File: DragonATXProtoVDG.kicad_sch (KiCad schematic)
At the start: 69 parts, among them IC1 74LS273, IC2 MC6847, IC3 MC14053, J1 Video Output, J2 Board Interconnect Male, J3 JTAG, Q1 MMBT4401, Q2 NPN, Q3 NPN, Q4 NPN, Q5 NPN, Q6 NPN, U1 AD724JR, U3 ATF1504ASL-xAx44, Y1 4.433620MHz

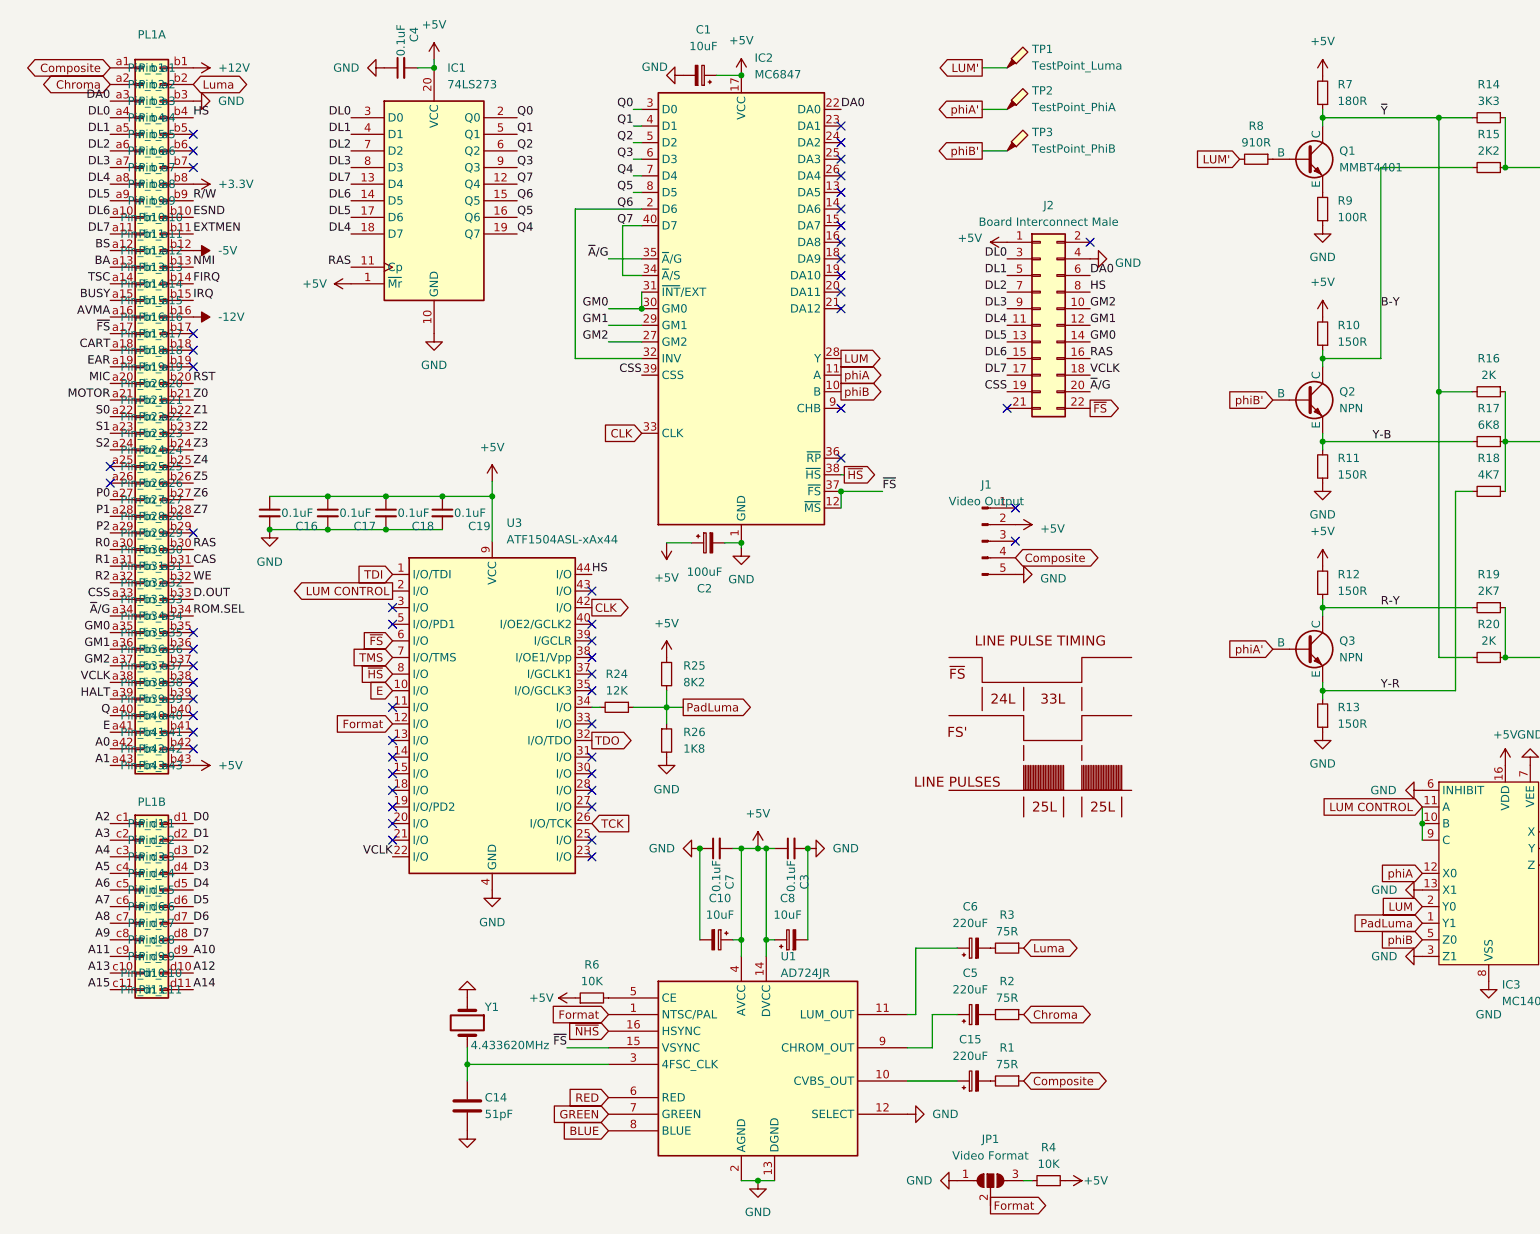
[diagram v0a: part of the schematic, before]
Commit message: refine design for ATF1504
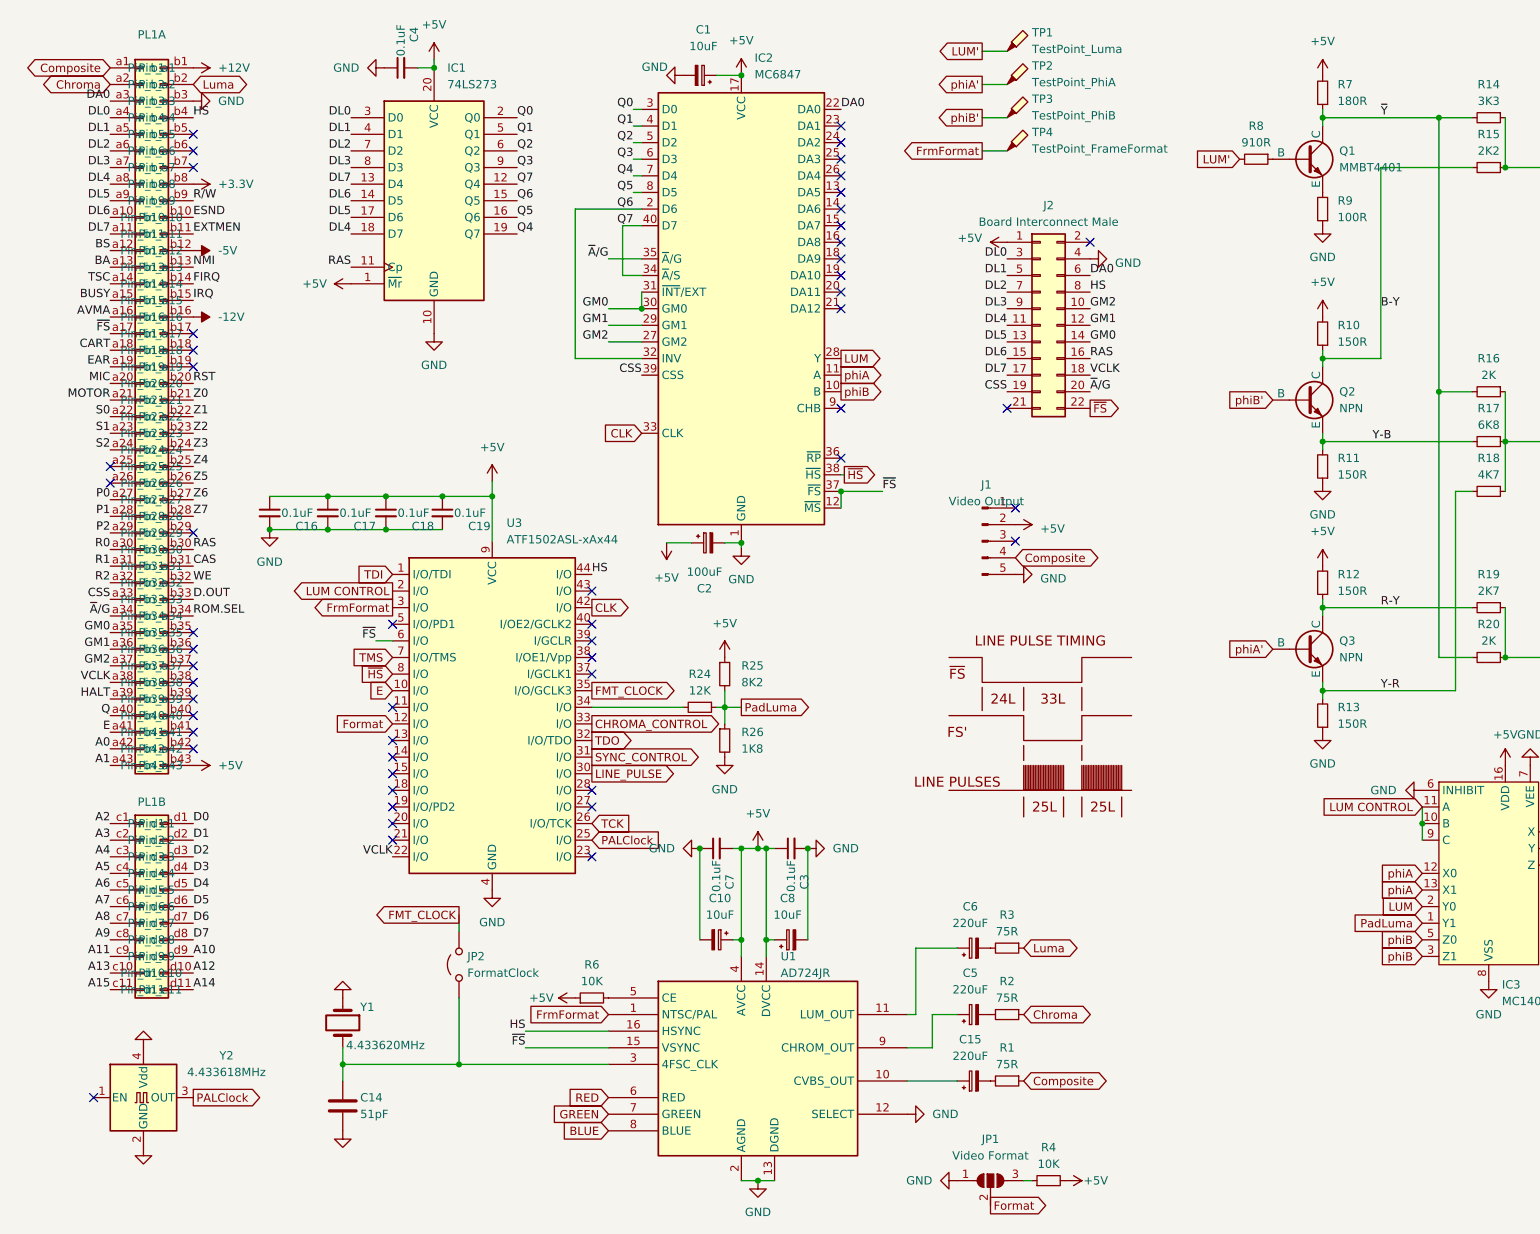
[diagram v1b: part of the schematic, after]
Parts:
- added JP2: FormatClock, Jumper:SolderJumper-2_P1.3mm_Open_Pad1.0x1.5mm, symbol Jumper:Jumper_2_Open
- added TP4: TestPoint_FrameFormat, TestPoint:TestPoint_Pad_D1.0mm, symbol Connector:TestPoint_Probe
- added Y2: 4.433618MHz, Oscillator:Oscillator_SMD_SeikoEpson_SG8002LB-4Pin_5.0x3.2mm_HandSoldering, symbol Oscillator:ASV-xxxMHz
- C15, C5, C6: footprint Capacitor_SMD:CP_Elec_4x5.4 -> Capacitor_Tantalum_SMD:CP_EIA-3216-12_Kemet-S; DigiKey 732-6401-1-ND -> 478-4922-1-ND
- U3: value ATF1504ASL-xAx44 -> ATF1502ASL-xAx44
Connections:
- net ~{NHS} is gone; now on net HS: U1.16 (HSYNC)
- net Format: no longer U1.1 (NTSC/PAL)
- net GND: now also Y2.2 (GND), Y2.4 (Vdd); no longer IC3.13 (X1), IC3.3 (Z1)
- net phiA: now also IC3.13 (X1)
- net phiB: now also IC3.3 (Z1)
- net at C14.1, U1.3 (4FSC_CLK), Y1.2: now also JP2.1 (A)
- net PALClock: now reaches U3.25 (I/O)
- net PALClock: now also Y2.3 (OUT)
- net FrmFormat: now reaches U3.3 (I/O)
- net FrmFormat: now also U1.1 (NTSC/PAL), TP4.1
- net LINE_PULSE: now reaches U3.30 (I/O)
- net SYNC_CONTROL: now reaches U3.31 (I/O)
- net CHROMA_CONTROL: now reaches U3.33 (I/O)
- net FMT_CLOCK: now reaches U3.35 (I/O/GCLK3)
- net FMT_CLOCK: now also JP2.2 (B)
- no-connect marks 60 -> 55
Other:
- moved on the sheet: C14, R24, R25, R26, TP1, TP2, TP3, Y1

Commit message: rework for path gates
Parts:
- removed C14: 51pF, Capacitor_SMD:C_0805_2012Metric, symbol Device:C
- removed J1: Video Output, Connector_PinHeader_2.54mm:PinHeader_1x05_P2.54mm_Vertical, symbol Connector:Conn_01x05_Pin
- removed J2: Board Interconnect Male, Connector_PinHeader_2.54mm:PinHeader_2x11_P2.54mm_Vertical, symbol Connector_Generic:Conn_02x11_Odd_Even
- removed JP2: FormatClock, Jumper:SolderJumper-2_P1.3mm_Open_Pad1.0x1.5mm, symbol Jumper:Jumper_2_Open
- removed Y1: 4.433620MHz, Crystal:Crystal_HC18-U_Vertical, symbol Device:Crystal
- added C14, C20, C9: 0.1uF, Capacitor_SMD:C_0805_2012Metric_Pad1.18x1.45mm_HandSolder, symbol Device:C_Small
- added U2, U4, U5: 74LS244, PCM_Package_SO_AKL:SO-20_5.3x12.6mm_P1.27mm, symbol 74xx:74LS244
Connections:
- net +5V: now also C14.2, C20.2, C9.2, U2.20 (VCC), U4.20 (VCC), U5.20 (VCC)
- net D0: now also U4.2 (I0a), U5.18 (O0a)
- net D1: now also U4.4 (I1a), U5.16 (O1a)
- net D2: now also U4.6 (I2a), U5.14 (O2a)
- net D3: now also U4.8 (I3a), U5.12 (O3a)
- net D4: now also U4.11 (I0b), U5.9 (O0b)
- net D5: now also U4.13 (I1b), U5.7 (O1b)
- net D6: now also U4.15 (I2b), U5.5 (O2b)
- net D7: now also U4.17 (I3b), U5.3 (O3b)
- net FMT_CLOCK: now also U1.3 (4FSC_CLK)
- net GND: now also IC3.11 (A), IC3.12 (X0), IC3.13 (X1), IC3.3 (Z1), IC3.5 (Z0), IC3.9 (C), C14.1, C20.1, C9.1, U2.1 (OEa), U2.10 (GND), U2.19 (OEb), U4.10 (GND), U4.19 (OEb), U5.10 (GND), U5.19 (OEb)
- net LUM CONTROL: no longer IC3.11 (A), IC3.9 (C)
- net Q0: now also U2.3 (O3b), U4.18 (O0a), U5.2 (I0a); no longer IC1.2 (Q0)
- net Q1: now also U2.16 (O1a), U4.16 (O1a), U5.4 (I1a); no longer IC1.5 (Q1)
- net Q2: now also U2.5 (O2b), U4.14 (O2a), U5.6 (I2a); no longer IC1.6 (Q2)
- net Q3: now also U2.9 (O0b), U4.12 (O3a), U5.8 (I3a); no longer IC1.9 (Q3)
- net Q4: now also U2.18 (O0a), U4.9 (O0b), U5.11 (I0b); no longer IC1.19 (Q7)
- net Q5: now also U2.14 (O2a), U4.7 (O1b), U5.13 (I1b); no longer IC1.16 (Q6)
- net Q6: now also U2.7 (O1b), U4.5 (O2b), U5.15 (I2b); no longer IC1.15 (Q5)
- net Q7: now also U2.12 (O3a), U4.3 (O3b), U5.17 (I3b); no longer IC1.12 (Q4)
- net phiA: no longer IC3.12 (X0), IC3.13 (X1)
- net phiA': no longer IC3.14 (X)
- net phiB: no longer IC3.3 (Z1), IC3.5 (Z0)
- net phiB': no longer IC3.4 (Z)
- net CHROMA_CONTROL: no longer names the net of U3.33 (I/O)
- net SYNC_CONTROL: no longer names the net of U3.31 (I/O)
- new net: IC1.9 (Q3), U2.11 (I0b)
- new net: IC1.15 (Q5), U2.13 (I1b)
- new net: IC1.6 (Q2), U2.15 (I2b)
- new net: IC1.2 (Q0), U2.17 (I3b)
- new net: IC1.19 (Q7), U2.2 (I0a)
- new net: IC1.5 (Q1), U2.4 (I1a)
- new net: IC1.16 (Q6), U2.6 (I2a)
- new net: IC1.12 (Q4), U2.8 (I3a)
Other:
- moved on the sheet: C1, C10, C11, C12, C13, C15, C16, C17, C18, C19, C2, C3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

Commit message: revise cpld logic
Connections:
- net phiA' is gone; now on net phiA: Q3.2 (B), TP2.1
- net phiB' is gone; now on net phiB: Q2.2 (B), TP3.1
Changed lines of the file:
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@@
 		)
 	)
-	(global_label "phiA'"
+	(global_label "phiA"
 		(shape input)
 		(at 309.88 114.3 180)
@@
 		)
 		(property "Intersheetrefs" "${INTERSHEET_REFS}"
-			(at 302.2986 114.3 0)
+			(at 302.9034 114.3 0)
 			(effects
 				(font
@@
 		)
 	)
-	(global_label "phiB'"
+	(global_label "phiB"
 		(shape output)
 		(at 265.43 269.24 180)
@@
 		)
 		(property "Intersheetrefs" "${INTERSHEET_REFS}"
-			(at 257.6672 269.24 0)
+			(at 258.272 269.24 0)
 			(effects
 				(font
@@
 		)
 	)
-	(global_label "phiA'"
+	(global_label "phiA"
 		(shape output)
 		(at 265.43 264.16 180)
@@
 		)
 		(property "Intersheetrefs" "${INTERSHEET_REFS}"
-			(at 257.8486 264.16 0)
+			(at 258.4534 264.16 0)
 			(effects
 				(font
@@
 		)
 	)
-	(global_label "phiB'"
+	(global_label "phiB"
 		(shape input)
 		(at 309.88 76.2 180)
@@
 		)
 		(property "Intersheetrefs" "${INTERSHEET_REFS}"
-			(at 302.1172 76.2 0)
-			(effects
-				(font
+			(at 302.722 76.2 0)
+			(effects
+				(font

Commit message: update
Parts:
- removed C14, C20, C9: 0.1uF, Capacitor_SMD:C_0805_2012Metric_Pad1.18x1.45mm_HandSolder, symbol Device:C_Small
- removed U2, U4, U5: 74LS244, PCM_Package_SO_AKL:SO-20_5.3x12.6mm_P1.27mm, symbol 74xx:74LS244
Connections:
- net E: no longer U3.10 (I/O)
- net Q0: now also IC1.2 (Q0)
- net Q1: now also IC1.5 (Q1)
- net Q2: now also IC1.6 (Q2)
- net Q3: now also IC1.9 (Q3)
- net Q4: now also IC1.19 (Q7)
- net Q5: now also IC1.16 (Q6)
- net Q6: now also IC1.15 (Q5)
- net Q7: now also IC1.12 (Q4)
- no-connect marks 55 -> 56
